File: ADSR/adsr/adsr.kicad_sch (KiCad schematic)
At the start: 45 parts, among them J1 PJ301M-12, J2 PJ301M-12, J3 EURO_PWR_2x5, Q1 BC547, Q2 BC547, Q3 BC547, U1 ICM7555xP, U2 LM358, U3 LM358

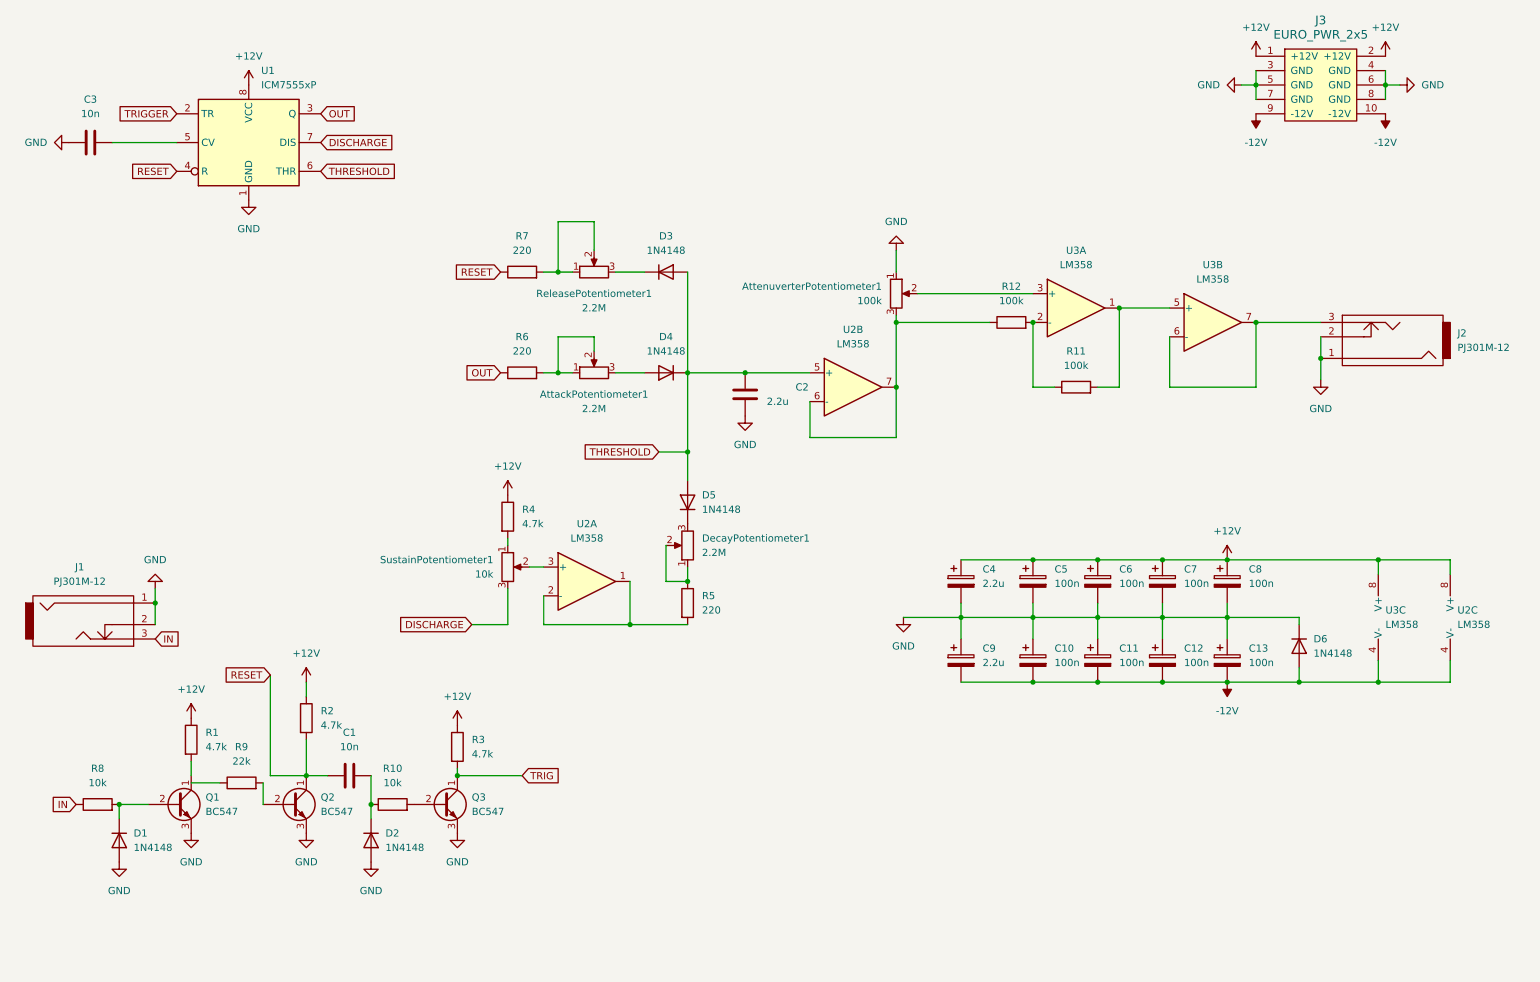
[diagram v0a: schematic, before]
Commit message: change schematic, add symbols and footprints
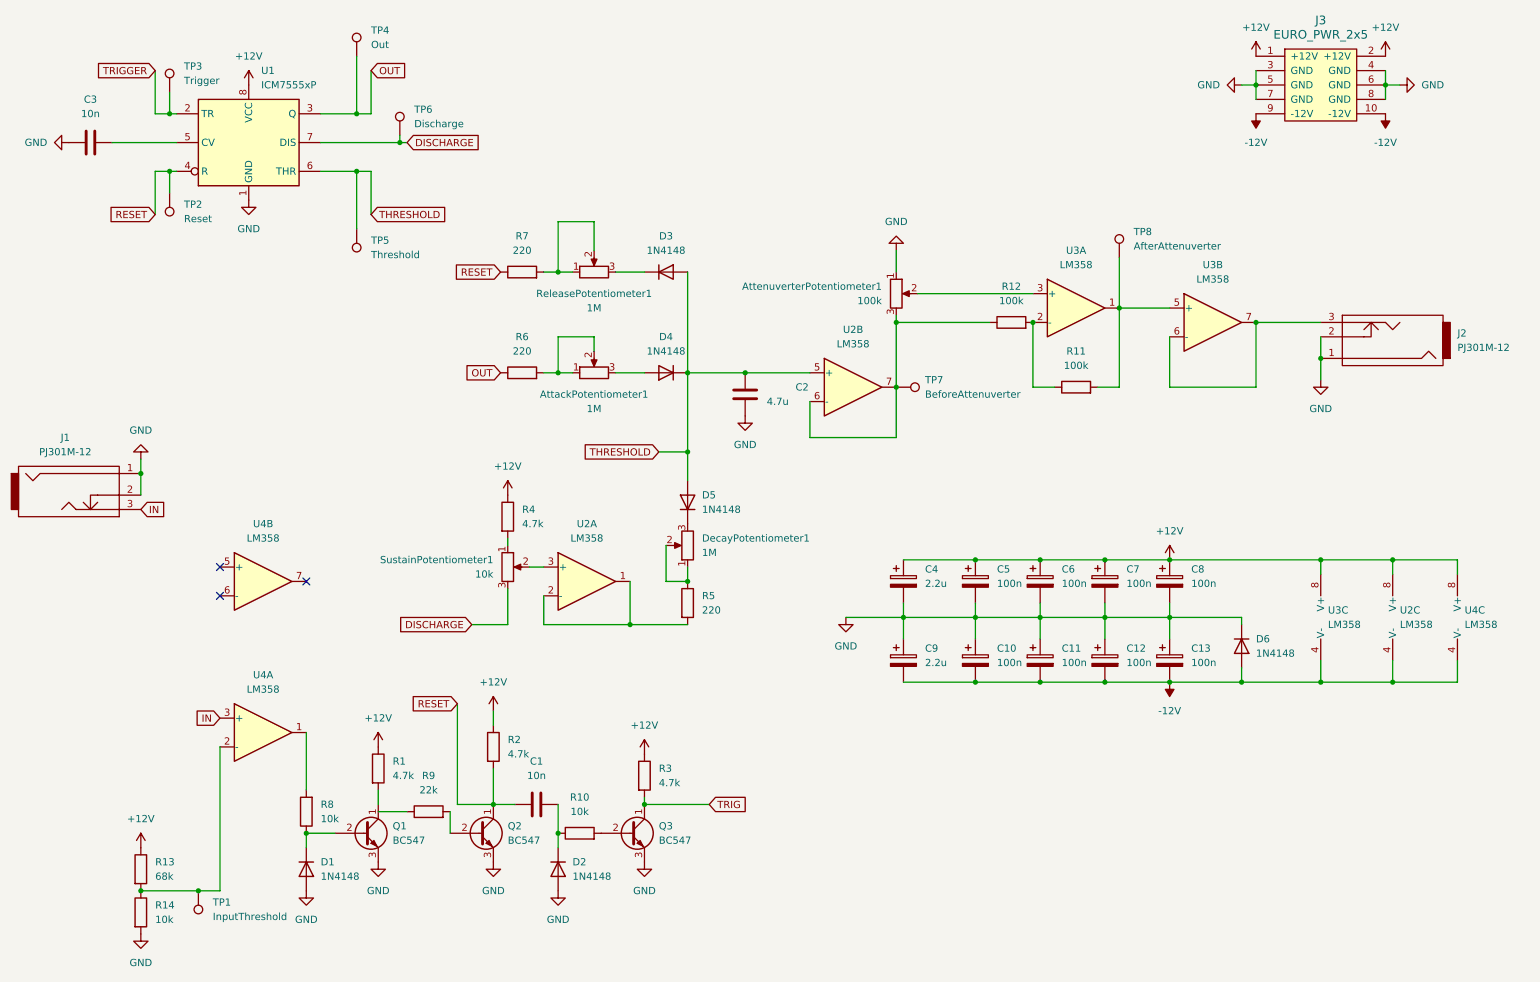
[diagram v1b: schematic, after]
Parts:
- added R13: 68k, symbol Device:R
- added R14: 10k, symbol Device:R
- added TP1: InputThreshold, TestPoint:TestPoint_Loop_D2.50mm_Drill1.0mm, symbol Connector:TestPoint
- added TP2: Reset, TestPoint:TestPoint_Loop_D2.50mm_Drill1.0mm, symbol Connector:TestPoint
- added TP3: Trigger, TestPoint:TestPoint_Loop_D2.50mm_Drill1.0mm, symbol Connector:TestPoint
- added TP4: Out, TestPoint:TestPoint_Loop_D2.50mm_Drill1.0mm, symbol Connector:TestPoint
- added TP5: Threshold, TestPoint:TestPoint_Loop_D2.50mm_Drill1.0mm, symbol Connector:TestPoint
- added TP6: Discharge, TestPoint:TestPoint_Loop_D2.50mm_Drill1.0mm, symbol Connector:TestPoint
- added TP7: BeforeAttenuverter, TestPoint:TestPoint_Loop_D2.50mm_Drill1.0mm, symbol Connector:TestPoint
- added TP8: AfterAttenuverter, TestPoint:TestPoint_Loop_D2.50mm_Drill1.0mm, symbol Connector:TestPoint
- added U4: LM358, symbol Amplifier_Operational:LM358
- AttackPotentiometer1, DecayPotentiometer1, ReleasePotentiometer1: value 2.2M -> 1M; footprint (none) -> Eurocad:Alpha9mmPot
- AttenuverterPotentiometer1, SustainPotentiometer1: footprint (none) -> Eurocad:Alpha9mmPot
- C2: value 2.2u -> 4.7u
- J1, J2: footprint (none) -> Eurocad:PJ301M-12
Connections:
- net +12V: now also R13.1, U4.8 (V+)
- net -12V: now also U4.4 (V-)
- net DISCHARGE: now also TP6.1
- net GND: now also R14.2
- net IN: now also U4.3 (+); no longer R8.1
- net OUT: now also TP4.1
- net RESET: now also TP2.1
- net THRESHOLD: now also TP5.1
- net TRIGGER: now also TP3.1
- net at D1.1 (K), Q1.2 (B): now also R8.1; no longer R8.2
- net at R11.2, U3.1, U3.5 (+): now also TP8.1
- net at AttenuverterPotentiometer1.3, R12.1, U2.6 (-)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: now also TP7.1
- new net: R13.2, R14.1, TP1.1, U4.2 (-)
- new net: R8.2, U4.1
- no-connect marks 0 -> 3
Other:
- moved on the sheet: C1, C10, C11, C12, C13, C4, C5, C6, C7, C8, C9, D1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

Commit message: more modules
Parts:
- C1, C10, C11, C12, C13, C2, C3, C4, C5, C6, C7, C8, C9: footprint (none) -> Capacitor_THT:C_Disc_D5.0mm_W2.5mm_P5.00mm
- Power1: renamed from J3; footprint (none) -> Connector_PinHeader_2.54mm:PinHeader_2x05_P2.54mm_Vertical
- R1, R10, R11, R12, R13, R14, R2, R3, R4, R5, R6, R7, R8, R9: footprint (none) -> Resistor_THT:R_Axial_DIN0207_L6.3mm_D2.5mm_P10.16mm_Horizontal
- U2, U3, U4: footprint (none) -> LM358PE3:DIP794W45P254L959H508Q8
- renumbered AttackPotentiometer1 to Attack1, AttenuverterPotentiometer1 to Attenuverter1, DecayPotentiometer1 to Decay1, J1 to Input1, J2 to Output1, ReleasePotentiometer1 to Release1, SustainPotentiometer1 to Sustain1
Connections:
- net at R9.1: now also Q1.1 (C), R1.2
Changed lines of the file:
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@@
 	)
 	(junction
+		(at 82.55 166.37)
+		(diameter 0)
+		(color 0 0 0 0)
+	)
+	(junction
 		(at 210.82 123.19)
 		(diameter 0)
@@
 	(wire
 		(pts
-			(xy 82.55 167.64) (xy 87.63 167.64)
-		)
-		(stroke
-			(width 0)
-			(type default)
-		)
-	)
-	(wire
-		(pts
 			(xy 69.85 171.45) (xy 74.93 171.45)
 		)
@@
 	(wire
 		(pts
+			(xy 82.55 167.64) (xy 82.55 166.37)
+		)
+		(stroke
+			(width 0)
+			(type default)
+		)
+	)
+	(wire
+		(pts
 			(xy 237.49 81.28) (xy 237.49 92.71)
 		)
@@
 	(wire
 		(pts
+			(xy 87.63 167.64) (xy 82.55 167.64)
+		)
+		(stroke
+			(width 0)
+			(type default)
+		)
+	)
+	(wire
+		(pts
 			(xy 234.95 39.37) (xy 237.49 39.37)
 		)
@@
 		(dnp no)
 		(fields_autoplaced yes)
-		(property "Reference" "J3"
+		(property "Reference" "Power1"
 			(at 248.92 27.94 0)
 			(effects
@@
 			)
 		)
-		(property "Footprint" ""
+		(property "Footprint" "Connector_PinHeader_2.54mm:PinHeader_2x05_P2.54mm_Vertical"
 			(at 248.92 39.37 0)
 			(effects
@@
 			(project ""
 				(path "/1ccaf6b8-14b3-446f-93e3-cfa1876ea6b7"
-					(reference "J3")
+					(reference "Power1")
 					(unit 1)
 				)
@@
 			)
 		)
-		(property "Footprint" ""
+		(property "Footprint" "LM358PE3:DIP794W45P254L959H508Q8"
 			(at 264.16 133.35 0)
 			(effects
@@
 		(dnp no)
 		(fields_autoplaced yes)
-		(property "Reference" "SustainPotentiometer1"
+		(property "Reference" "Sustain1"
 			(at 102.87 123.1899 0)
 			(effects
@@
 			(project "adsr"
 				(path "/1ccaf6b8-14b3-446f-93e3-cfa1876ea6b7"
-					(reference "SustainPotentiometer1")
+					(reference "Sustain1")
 					(unit 1)
 				)
@@
 			)
 		)
-		(property "Footprint" ""
+		(property "Footprint" "Capacitor_THT:C_Disc_D5.0mm_W2.5mm_P5.00mm"
 			(at 106.68 167.3352 0)
 			(effects
@@
 		(dnp no)
 		(fields_autoplaced yes)
-		(property "Reference" "ReleasePotentiometer1"
+		(property "Reference" "Release1"
 			(at 120.65 76.2 90)
 			(effects
@@
 			(project ""
 				(path "/1ccaf6b8-14b3-446f-93e3-cfa1876ea6b7"
-					(reference "ReleasePotentiometer1")
+					(reference "Release1")
 					(unit 1)
 				)
@@
 			)
 		)
-		(property "Footprint" ""
+		(property "Footprint" "Resistor_THT:R_Axial_DIN0207_L6.3mm_D2.5mm_P10.16mm_Horizontal"
 			(at 91.44 169.418 90)
 			(effects
@@
 			)
 		)
-		(property "Footprint" ""
+		(property "Footprint" "Resistor_THT:R_Axial_DIN0207_L6.3mm_D2.5mm_P10.16mm_Horizontal"
 			(at 205.74 94.488 90)
 			(effects
@@
 			)
 		)
-		(property "Footprint" ""
+		(property "Footprint" "LM358PE3:DIP794W45P254L959H508Q8"
 			(at 205.74 78.74 0)
 			(effects
@@
 			)
 		)
-		(property "Footprint" ""
+		(property "Footprint" "Capacitor_THT:C_Disc_D5.0mm_W2.5mm_P5.00mm"
 			(at 188.9252 130.81 0)
 			(effects
@@
 			)
 		)
-		(property "Footprint" ""
+		(property "Footprint" "Resistor_THT:R_Axial_DIN0207_L6.3mm_D2.5mm_P10.16mm_Horizontal"
 			(at 38.862 185.42 90)
 			(effects
@@
 			)
 		)
-		(property "Footprint" ""
+		(property "Footprint" "Capacitor_THT:C_Disc_D5.0mm_W2.5mm_P5.00mm"
 			(at 211.7852 144.78 0)
 			(effects
@@
 			)
 		)
-		(property "Footprint" ""
+		(property "Footprint" "Capacitor_THT:C_Disc_D5.0mm_W2.5mm_P5.00mm"
 			(at 223.2152 144.78 0)
 			(effects
@@
 			)
 		)
-		(property "Footprint" ""
+		(property "Footprint" "Capacitor_THT:C_Disc_D5.0mm_W2.5mm_P5.00mm"
 			(at 27.94 50.4952 0)
 			(effects
@@
 			)
 		)
-		(property "Footprint" ""
+		(property "Footprint" "Capacitor_THT:C_Disc_D5.0mm_W2.5mm_P5.00mm"
 			(at 200.3552 130.81 0)
 			(effects
@@
 			)
 		)
-		(property "Footprint" ""
+		(property "Footprint" "Resistor_THT:R_Axial_DIN0207_L6.3mm_D2.5mm_P10.16mm_Horizontal"
 			(at 107.95 91.948 90)
 			(effects
@@
 			)
 		)
-		(property "Footprint" ""
+		(property "Footprint" "Resistor_THT:R_Axial_DIN0207_L6.3mm_D2.5mm_P10.16mm_Horizontal"
 			(at 71.628 167.64 90)
 			(effects
@@
 			)
 		)
-		(property "Footprint" ""
+		(property "Footprint" "Resistor_THT:R_Axial_DIN0207_L6.3mm_D2.5mm_P10.16mm_Horizontal"
 			(at 80.772 160.02 90)
 			(effects
@@
 			)
 		)
-		(property "Footprint" ""
+		(property "Footprint" "Resistor_THT:R_Axial_DIN0207_L6.3mm_D2.5mm_P10.16mm_Horizontal"
 			(at 194.31 83.058 90)
 			(effects
@@
 			)
 		)
-		(property "Footprint" ""
+		(property "Footprint" "LM358PE3:DIP794W45P254L959H508Q8"
 			(at 62.23 127 0)
 			(effects
@@
 			)
 		)
-		(property "Footprint" ""
+		(property "Footprint" "Capacitor_THT:C_Disc_D5.0mm_W2.5mm_P5.00mm"
 			(at 146.3548 90.17 0)
 			(effects
@@
 		(dnp no)
 		(fields_autoplaced yes)
-		(property "Reference" "J2"
+		(property "Reference" "Output1"
 			(at 273.05 83.1849 0)
 			(effects
@@
 			(project "adsr"
 				(path "/1ccaf6b8-14b3-446f-93e3-cfa1876ea6b7"
-					(reference "J2")
+					(reference "Output1")
 					(unit 1)
 				)
@@
 			)
 		)
-		(property "Footprint" ""
+		(property "Footprint" "Resistor_THT:R_Axial_DIN0207_L6.3mm_D2.5mm_P10.16mm_Horizontal"
 			(at 118.11 173.228 90)
 			(effects
@@
 			)
 		)
-		(property "Footprint" ""
+		(property "Footprint" "Capacitor_THT:C_Disc_D5.0mm_W2.5mm_P5.00mm"
 			(at 188.9252 144.78 0)
 			(effects
@@
 			)
 		)
-		(property "Footprint" ""
+		(property "Footprint" "LM358PE3:DIP794W45P254L959H508Q8"
 			(at 275.59 133.35 0)
 			(effects
@@
 			)
 		)
-		(property "Footprint" ""
+		(property "Footprint" "Resistor_THT:R_Axial_DIN0207_L6.3mm_D2.5mm_P10.16mm_Horizontal"
 			(at 127.762 161.29 90)
 			(effects
@@
 			)
 		)
-		(property "Footprint" ""
+		(property "Footprint" "LM358PE3:DIP794W45P254L959H508Q8"
 			(at 166.37 92.71 0)
 			(effects
@@
 			)
 		)
-		(property "Footprint" ""
+		(property "Footprint" "Capacitor_THT:C_Disc_D5.0mm_W2.5mm_P5.00mm"
 			(at 211.7852 130.81 0)
 			(effects
@@
 			)
 		)
-		(property "Footprint" ""
+		(property "Footprint" "Resistor_THT:R_Axial_DIN0207_L6.3mm_D2.5mm_P10.16mm_Horizontal"
 			(at 38.862 177.8 90)
 			(effects
@@
 		(dnp no)
 		(fields_autoplaced yes)
-		(property "Reference" "AttackPotentiometer1"
+		(property "Reference" "Attack1"
 			(at 120.65 93.98 90)
 			(effects
@@
 			(project "adsr"
 				(path "/1ccaf6b8-14b3-446f-93e3-cfa1876ea6b7"
-					(reference "AttackPotentiometer1")
+					(reference "Attack1")
 					(unit 1)
 				)
@@
 			)
 		)
-		(property "Footprint" ""
+		(property "Footprint" "Resistor_THT:R_Axial_DIN0207_L6.3mm_D2.5mm_P10.16mm_Horizontal"
 			(at 103.632 115.57 90)
 			(effects
@@
 		(dnp no)
 		(fields_autoplaced yes)
-		(property "Reference" "AttenuverterPotentiometer1"
+		(property "Reference" "Attenuverter1"
 			(at 171.45 74.9299 0)
 			(effects
@@
 			(project "adsr"
 				(path "/1ccaf6b8-14b3-446f-93e3-cfa1876ea6b7"
-					(reference "AttenuverterPotentiometer1")
+					(reference "Attenuverter1")
 					(unit 1)
 				)
@@
 			)
 		)
-		(property "Footprint" ""
+		(property "Footprint" "Capacitor_THT:C_Disc_D5.0mm_W2.5mm_P5.00mm"
 			(at 200.3552 144.78 0)
 			(effects
@@
 		(dnp no)
 		(fields_autoplaced yes)
-		(property "Reference" "J1"
+		(property "Reference" "Input1"
 			(at 27.305 101.6 0)
 			(effects
@@
 			(project ""
 				(path "/1ccaf6b8-14b3-446f-93e3-cfa1876ea6b7"
-					(reference "J1")
+					(reference "Input1")
 					(unit 1)
 				)
@@
 			)
 		)
-		(property "Footprint" ""
+		(property "Footprint" "LM358PE3:DIP794W45P254L959H508Q8"
 			(at 229.87 81.28 0)
 			(effects
@@
 		(dnp no)
 		(fields_autoplaced yes)
-		(property "Reference" "DecayPotentiometer1"
+		(property "Reference" "Decay1"
 			(at 139.7 119.3799 0)
 			(effects
@@
 			(project "adsr"
 				(path "/1ccaf6b8-14b3-446f-93e3-cfa1876ea6b7"
-					(reference "DecayPotentiometer1")
+					(reference "Decay1")
 					(unit 1)
 				)
@@
 			)
 		)
-		(property "Footprint" ""
+		(property "Footprint" "LM358PE3:DIP794W45P254L959H508Q8"
 			(at 251.46 133.35 0)
 			(effects
@@
 			)
 		)
-		(property "Footprint" ""
+		(property "Footprint" "Capacitor_THT:C_Disc_D5.0mm_W2.5mm_P5.00mm"
 			(at 176.2252 130.81 0)
 			(effects
@@
 			)
 		)
-		(property "Footprint" ""
+		(property "Footprint" "Resistor_THT:R_Axial_DIN0207_L6.3mm_D2.5mm_P10.16mm_Horizontal"
 			(at 101.092 156.21 90)
 			(effects
@@
 			)
 		)
-		(property "Footprint" ""
+		(property "Footprint" "Capacitor_THT:C_Disc_D5.0mm_W2.5mm_P5.00mm"
 			(at 176.2252 144.78 0)
 			(effects
@@
 			)
 		)
-		(property "Footprint" ""
+		(property "Footprint" "Capacitor_THT:C_Disc_D5.0mm_W2.5mm_P5.00mm"
 			(at 223.2152 130.81 0)
 			(effects
@@
 			)
 		)
-		(property "Footprint" ""
+		(property "Footprint" "LM358PE3:DIP794W45P254L959H508Q8"
 			(at 119.38 127 0)
 			(effects
@@
 			)
 		)
-		(property "Footprint" ""
+		(property "Footprint" "Resistor_THT:R_Axial_DIN0207_L6.3mm_D2.5mm_P10.16mm_Horizontal"
 			(at 107.95 74.168 90)
 			(effects
@@
 			)
 		)
-		(property "Footprint" ""
+		(property "Footprint" "LM358PE3:DIP794W45P254L959H508Q8"
 			(at 62.23 153.67 0)
 			(effects
@@
 			)
 		)
-		(property "Footprint" ""
+		(property "Footprint" "Resistor_THT:R_Axial_DIN0207_L6.3mm_D2.5mm_P10.16mm_Horizontal"
 			(at 135.382 130.81 90)
 			(effects
